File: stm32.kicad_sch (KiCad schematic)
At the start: 68 parts, among them J1 SWD, J2 USB_C_Receptacle_USB2.0_16P, J3 I²C1, J4 SPI1, J5 UART2_3V3, J6 ANALOG_3V3, J7 GPIO_D, J8 EXPANSION_3V3, SW1 SW_Push_Open, SW2 SW_Push_Open, SW3 SW_Push_Open, U1 STM32F446ZETx, U2 USBLC6-2SC6, U3 TPS7A2533DRVR, U4 TPS22918DBVR, Y1 8MHz

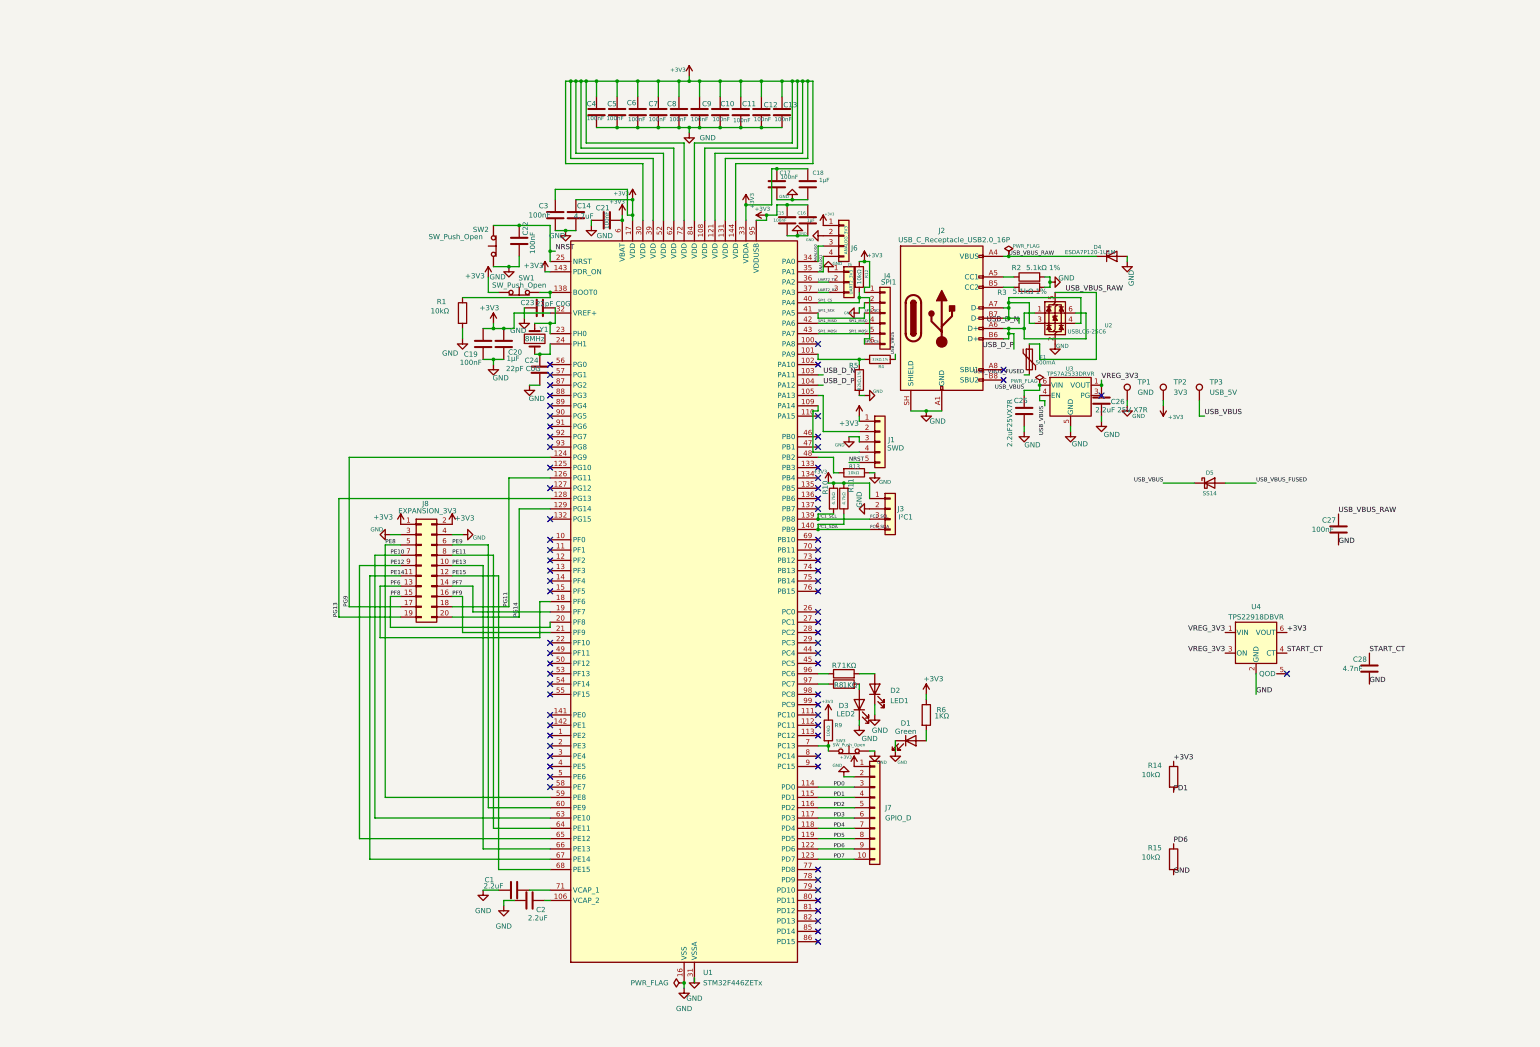
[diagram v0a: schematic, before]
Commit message: Organize schematic into functional sheets with verified pin mapping
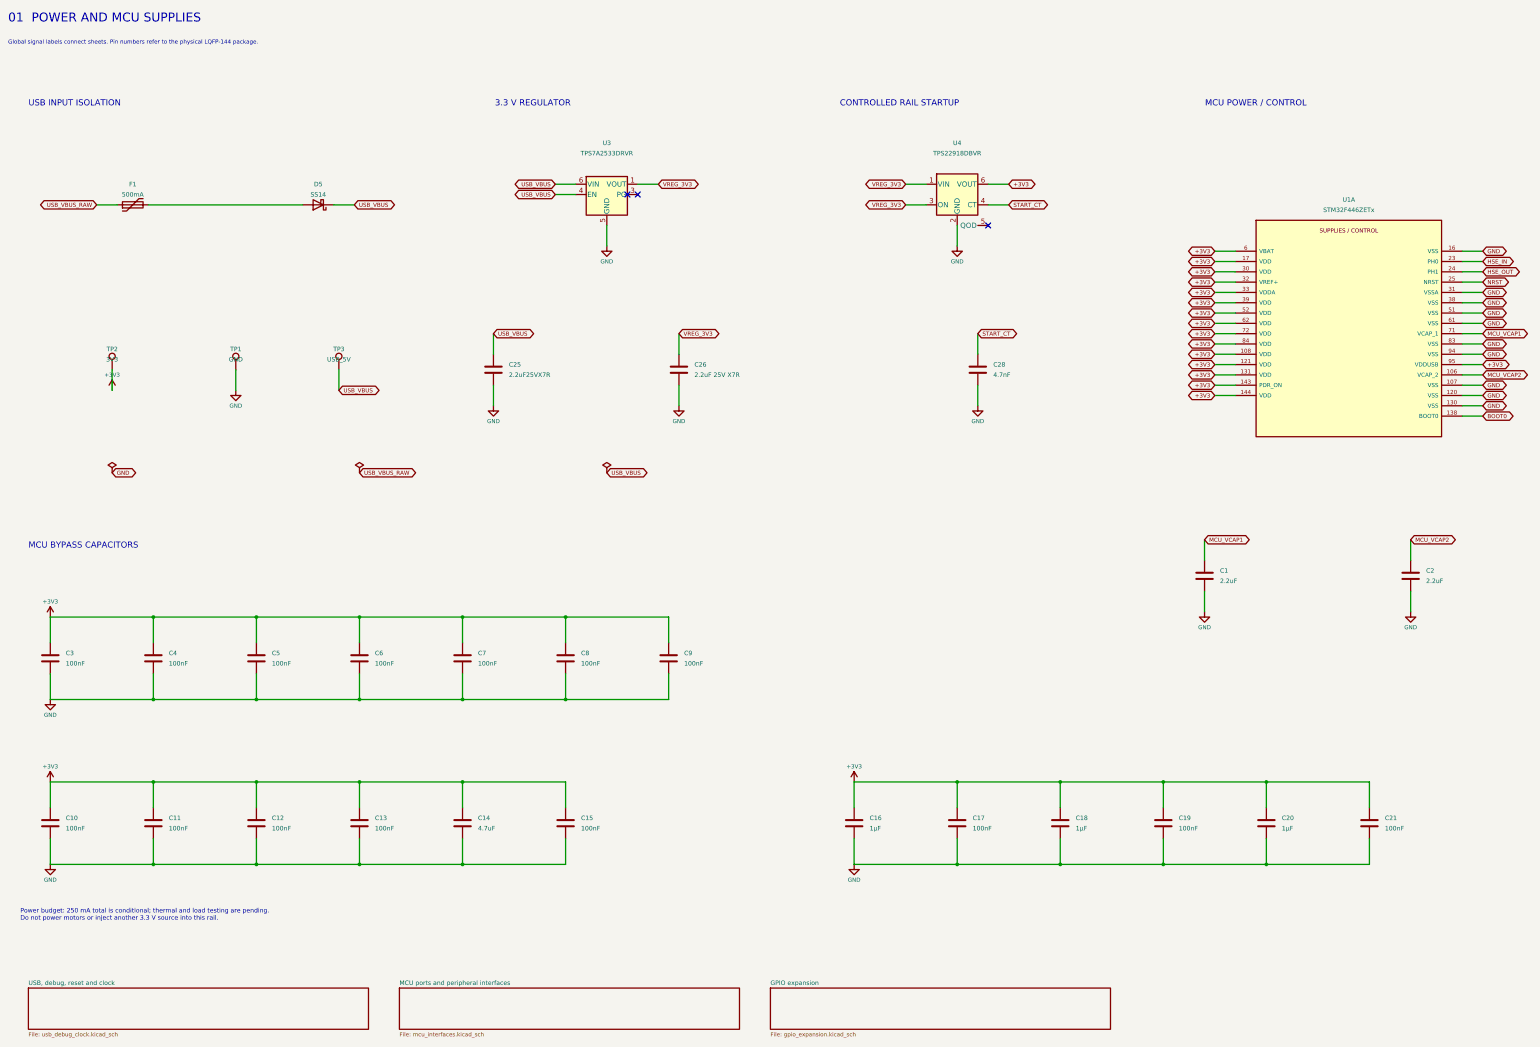
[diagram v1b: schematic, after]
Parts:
- removed C22, C27: 100nF, Capacitor_SMD:C_0805_2012Metric, symbol Device:C
- removed C23, C24: 22pF C0G, Capacitor_SMD:C_0805_2012Metric, symbol Device:C
- removed D1: Green, LED_SMD:LED_0805_2012Metric, symbol Device:LED
- removed D2: LED1, LED_SMD:LED_0805_2012Metric, symbol Device:LED
- removed D3: LED2, LED_SMD:LED_0805_2012Metric, symbol Device:LED
- removed D4: ESDA7P120-1U1M, STM32_Custom:ESDA7P60-1U1M, symbol STM32_Power:ESDA7P120_1U1M
- removed J1: SWD, Connector_PinHeader_2.54mm:PinHeader_1x05_P2.54mm_Vertical, symbol Connector_Generic:Conn_01x05
- removed J2: USB_C_Receptacle_USB2.0_16P, STM32_Custom:USB_C_Receptacle_USB4105_JLC, symbol Connector:USB_C_Receptacle_USB2.0_16P
- removed J3: I²C1, Connector_PinHeader_2.54mm:PinHeader_1x04_P2.54mm_Vertical, symbol Connector_Generic:Conn_01x04
- removed J4: SPI1, Connector_PinHeader_2.54mm:PinHeader_1x06_P2.54mm_Vertical, symbol Connector_Generic:Conn_01x06
- removed J5: UART2_3V3, Connector_PinHeader_2.54mm:PinHeader_1x03_P2.54mm_Vertical, symbol Connector_Generic:Conn_01x03
- removed J6: ANALOG_3V3, Connector_PinHeader_2.54mm:PinHeader_1x04_P2.54mm_Vertical, symbol Connector_Generic:Conn_01x04
- removed J7: GPIO_D, Connector_PinHeader_2.54mm:PinHeader_1x10_P2.54mm_Vertical, symbol Connector_Generic:Conn_01x10
- removed J8: EXPANSION_3V3, Connector_PinHeader_2.54mm:PinHeader_2x10_P2.54mm_Vertical, symbol Connector_Generic:Conn_02x10_Odd_Even
- removed R1, R12, R13, R14, R15, R9: 10kΩ, Resistor_SMD:R_0805_2012Metric, symbol Device:R
- removed R10, R11: 4.7kΩ, Resistor_SMD:R_0805_2012Metric, symbol Device:R
- removed R2, R3: 5.1kΩ 1%, Resistor_SMD:R_0805_2012Metric, symbol Device:R
- removed R4: 33kΩ,1%, Resistor_SMD:R_0805_2012Metric, symbol Device:R
- removed R5: 82kΩ,1%, Resistor_SMD:R_0805_2012Metric, symbol Device:R
- removed R6, R7, R8: 1KΩ, Resistor_SMD:R_0805_2012Metric, symbol Device:R
- removed SW1, SW2, SW3: SW_Push_Open, Button_Switch_THT:SW_PUSH_6mm_H4.3mm, symbol Switch:SW_Push_Open
- removed U2: USBLC6-2SC6, Package_TO_SOT_SMD:SOT-23-6, symbol Power_Protection:USBLC6-2SC6
- removed Y1: 8MHz, Crystal:Crystal_SMD_Abracon_ABM3-2Pin_5.0x3.2mm, symbol Device:Crystal
- U1: symbol MCU_ST_STM32F4:STM32F446ZETx -> STM32_MCU:STM32F446ZETx_Readable
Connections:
- net MCU_VCAP2: now reaches C2.1, U1.106 (VCAP_2)
- net BOOT0: now reaches U1.138 (BOOT0)
- net HSE_IN: now reaches U1.23 (PH0)
- net HSE_OUT: now reaches U1.24 (PH1)
- net MCU_VCAP1: now reaches C1.2, U1.71 (VCAP_1)
- removed net ANALOG0: U1.34 (PA0)
- removed net ANALOG1: U1.35 (PA1)
- removed net I²C1_SCL: U1.139 (PB8)
- removed net I²C1_SDA: U1.140 (PB9)
- removed net PD0: U1.114 (PD0)
- removed net PD1: U1.115 (PD1)
- removed net PD2: U1.116 (PD2)
- removed net PD3: U1.117 (PD3)
- removed net PD4: U1.118 (PD4)
- removed net PD5: U1.119 (PD5)
- removed net PD6: U1.122 (PD6)
- removed net PD7: U1.123 (PD7)
- removed net PE10: U1.63 (PE10)
- removed net PE11: U1.64 (PE11)
- removed net PE12: U1.65 (PE12)
- removed net PE13: U1.66 (PE13)
- removed net PE14: U1.67 (PE14)
- removed net PE15: U1.68 (PE15)
- removed net PE8: U1.59 (PE8)
- removed net PE9: U1.60 (PE9)
- removed net PF6: U1.18 (PF6)
- removed net PF7: U1.19 (PF7)
- removed net PF8: U1.20 (PF8)
- removed net PF9: U1.21 (PF9)
- removed net PG11: U1.126 (PG11)
- removed net PG13: U1.128 (PG13)
- removed net PG14: U1.129 (PG14)
- removed net PG9: U1.124 (PG9)
- removed net SPI1_CS: U1.40 (PA4)
- removed net SPI1_MISO: U1.42 (PA6)
- removed net SPI1_MOSI: U1.43 (PA7)
- removed net SPI1_SCK: U1.41 (PA5)
- removed net UART2_RX: U1.37 (PA3)
- removed net UART2_TX: U1.36 (PA2)
- removed net USB_D_N: U1.103 (PA11)
- removed net USB_D_P: U1.104 (PA12)
- net USB_VBUS_FUSED: no longer names the net of D5.2 (A), F1.2
- no-connect marks 73 -> 3
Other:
- added sheet GPIO expansion (gpio_expansion.kicad_sch)
- added sheet MCU ports and peripheral interfaces (mcu_interfaces.kicad_sch)
- added sheet USB, debug, reset and clock (usb_debug_clock.kicad_sch)
- note added: "01 POWER AND MCU SUPPLIES"
- note added: "3.3 V REGULATOR"
- note added: "CONTROLLED RAIL STARTUP"
- note added: "Global signal labels connect sheets. Pin numbers refer to the physical LQFP-144 package."
- note added: "MCU BYPASS CAPACITORS"
- note added: "MCU POWER / CONTROL"
- note added: "Power budget: 250 mA total is conditional; thermal and load testing are pending. Do not power motors or inject another 3.3 V source into this rail."
- note added: "USB INPUT ISOLATION"
- title: My_Custom_stm32 -> STM32F446 | Power and MCU supplies
- moved on the sheet: C1, C10, C11, C12, C13, C14, C15, C16, C17, C18, C19, C2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

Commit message: Publish corrected prototype package and documented engineering review
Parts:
- added C29: 1µF, Capacitor_SMD:C_0603_1608Metric, symbol Device:C
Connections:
- net GND: now also C29.2
- net VREG_3V3: now also C29.1
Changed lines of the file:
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@@
 	)
 	(junction
+		(at 238.76 55.88)
+		(diameter 0)
+		(color 0 0 0 0)
+	)
+	(junction
 		(at 274.32 223.52)
 		(diameter 0)
@@
 	(wire
 		(pts
+			(xy 238.76 53.34) (xy 238.76 55.88)
+		)
+		(stroke
+			(width 0)
+			(type default)
+		)
+	)
+	(wire
+		(pts
 			(xy 317.5 97.79) (xy 312.42 97.79)
 		)
@@
 	(wire
 		(pts
+			(xy 238.76 55.88) (xy 236.22 55.88)
+		)
+		(stroke
+			(width 0)
+			(type default)
+		)
+	)
+	(wire
+		(pts
 			(xy 162.56 66.04) (xy 162.56 71.12)
 		)
@@
 	(wire
 		(pts
+			(xy 217.17 55.88) (xy 217.17 53.34)
+		)
+		(stroke
+			(width 0)
+			(type default)
+		)
+	)
+	(wire
+		(pts
 			(xy 25.4 203.2) (xy 50.8 203.2)
 		)
@@
 	(wire
 		(pts
+			(xy 217.17 53.34) (xy 238.76 53.34)
+		)
+		(stroke
+			(width 0)
+			(type default)
+		)
+	)
+	(wire
+		(pts
 			(xy 50.8 217.17) (xy 50.8 223.52)
 		)
@@
 	(wire
 		(pts
+			(xy 217.17 63.5) (xy 217.17 64.77)
+		)
+		(stroke
+			(width 0)
+			(type default)
+		)
+	)
+	(wire
+		(pts
 			(xy 317.5 107.95) (xy 312.42 107.95)
 		)
@@
 	(wire
 		(pts
-			(xy 241.3 55.88) (xy 236.22 55.88)
+			(xy 241.3 55.88) (xy 238.76 55.88)
 		)
 		(stroke
@@
 	)
 	(symbol
+		(lib_id "power:GND")
+		(at 217.17 64.77 0)
+		(unit 1)
+		(body_style 1)
+		(exclude_from_sim no)
+		(in_bom yes)
+		(on_board yes)
+		(in_pos_files yes)
+		(dnp no)
+		(property "Reference" "#PWR0134"
+			(at 217.17 68.58 0)
+			(hide yes)
+			(show_name no)
+			(do_not_autoplace no)
+			(effects
+				(font
+					(size 1.27 1.27)
+				)
+			)
+		)
+		(property "Value" "GND"
+			(at 217.17 68.58 0)
+			(show_name no)
+			(do_not_autoplace no)
+			(effects
+				(font
+					(size 1 1)
+				)
+			)
+		)
+		(property "Footprint" "Package_TO_SOT_SMD:SOT-23-5"
+			(at 217.17 68.58 0)
+			(hide yes)
+			(show_name no)
+			(do_not_autoplace no)
+			(effects
+				(font
+					(size 1.27 1.27)
+				)
+			)
+		)
+		(property "Datasheet" ""
+			(at 217.17 68.58 0)
+			(hide yes)
+			(show_name no)
+			(do_not_autoplace no)
+			(effects
+				(font
+					(size 1.27 1.27)
+				)
+			)
+		)
+		(property "Description" "Power symbol creates a global label with name \"GND\" , ground"
+			(at 217.17 68.58 0)
+			(hide yes)
+			(show_name no)
+			(do_not_autoplace no)
+			(effects
+				(font
+					(size 1.27 1.27)
+				)
+			)
+		)
+		(pin "1"
+		)
+		(instances
+			(project "stm32"
+				(path "/20b47cb4-a94d-429e-be74-f8ca0a6c312b"
+					(reference "#PWR0134")
+					(unit 1)
+				)
+			)
+		)
+	)
+	(symbol
 		(lib_id "Device:D_Schottky")
 		(at 91.44 60.96 180)
@@
 					(unit 1)
 				)
+			)
+		)
+	)
+	(symbol
+		(lib_id "Device:C")
+		(at 217.17 59.69 0)
+		(unit 1)
+		(body_style 1)
+		(exclude_from_sim no)
+		(in_bom yes)
+		(on_board yes)
+		(in_pos_files yes)
+		(dnp no)
+		(fields_autoplaced yes)
+		(property "Reference" "C29"
+			(at 220.98 58.4199 0)
+			(show_name no)
+			(do_not_autoplace no)
+			(effects
+				(font
+					(size 1.27 1.27)
+				)
+				(justify left)
+			)
+		)
+		(property "Value" "1µF"
+			(at 220.98 60.9599 0)
+			(show_name no)
+			(do_not_autoplace no)
+			(effects
+				(font
+					(size 1.27 1.27)
+				)
+				(justify left)
+			)
+		)
+		(property "Footprint" "Capacitor_SMD:C_0603_1608Metric"
+			(at 218.1352 63.5 0)
+			(hide yes)
+			(show_name no)
+			(do_not_autoplace no)
+			(effects
+				(font
+					(size 1.27 1.27)
+				)
+			)
+		)
+		(property "Datasheet" ""
+			(at 217.17 59.69 0)
+			(hide yes)
+			(show_name no)
+			(do_not_autoplace no)
+			(effects
+				(font
+					(size 1.27 1.27)
+				)
+			)
+		)
+		(property "Description" "Unpolarized capacitor"
+			(at 217.17 59.69 0)
+			(hide yes)
+			(show_name no)
+			(do_not_autoplace no)
+			(effects
+				(font
+					(size 1.27 1.27)
+				)
+			)
+		)
+		(property "Manufacturer" "Samsung Electro-Mechanics"
+			(at 217.17 59.69 0)
+			(hide yes)
+			(show_name no)
+			(do_not_autoplace no)
+			(effects
+				(font
+					(size 1.27 1.27)
+				)
+			)
+		)
+		(property "Manufacturer Part Number" "CL10B105KA8NNNC"
+			(at 217.17 59.69 0)
+			(hide yes)
+			(show_name no)
+			(do_not_autoplace no)
+			(effects
+				(font
+					(size 1.27 1.27)
+				)
+			)
+		)
+		(property "LCSC Part Number" "C29936"
+			(at 217.17 59.69 0)
+			(hide yes)
+			(show_name no)
+			(do_not_autoplace no)
+			(effects
+				(font
+					(size 1.27 1.27)
+				)
+			)
+		)
+		(pin "2"
+		)
+		(pin "1"
+		)
+		(instances
+			(project "stm32"
+				(path "/20b47cb4-a94d-429e-be74-f8ca0a6c312b"
+					(reference "C29")
+					(unit 1)
+				)
